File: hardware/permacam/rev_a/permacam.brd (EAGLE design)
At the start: 27 x 60 mm, 96 parts, among them J1 TC2030-JLINK-NL, Q1 PMDXB950UPEL, Q2 PMDXB950UPEL, Q3 PMDXB950UPEL, Q4 PMDXB950UPEL, Q5 PMDXB950UPEL, Q6 PMDXB950UPEL, U1 AB1815-T3, U10 NRF52840, U2 BQ25505, U3 EKMB1101111, U4 HM01B0-ANA, U6 SN74AUP2G04DCKRDCK6-L, U7 MAX17222, U8 MAX44009, X1 32MHz, X3 32.768kHz, X4 ABS07-32.768KHZ-7-T

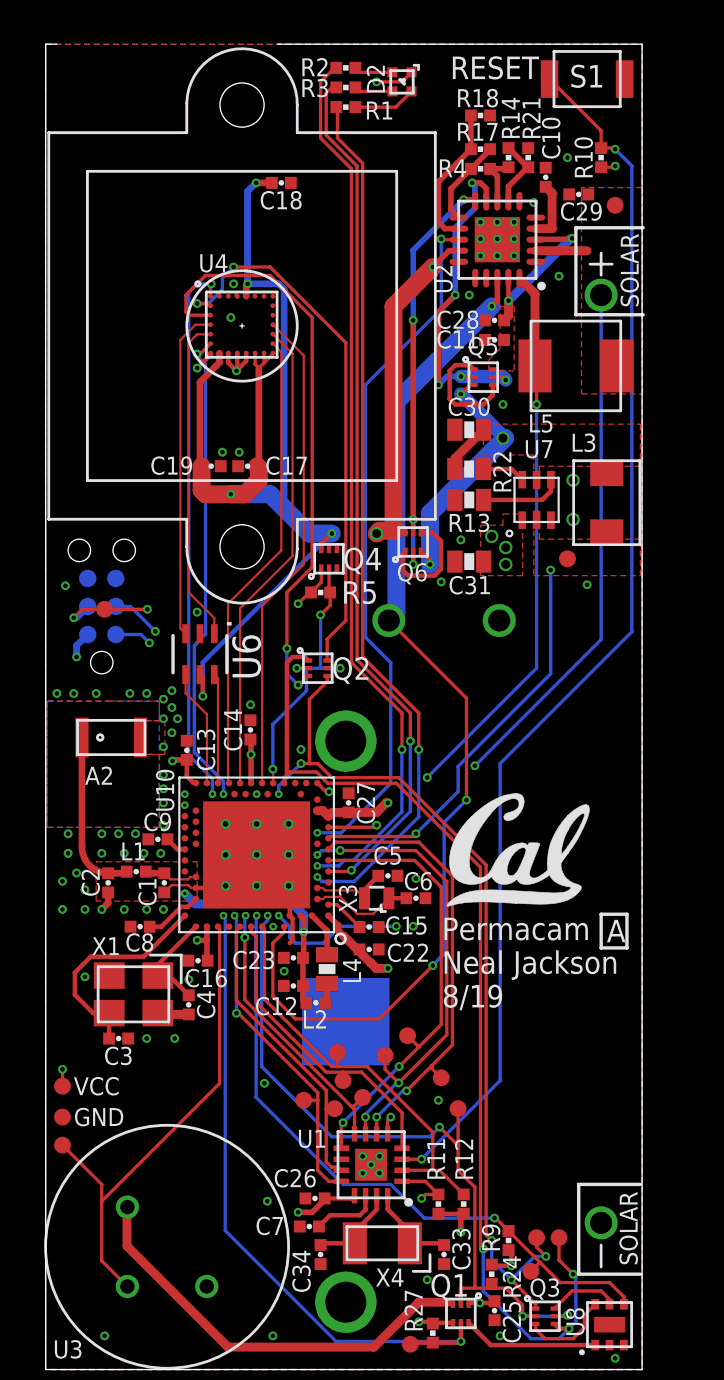
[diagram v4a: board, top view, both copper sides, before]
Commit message: fix exti floating
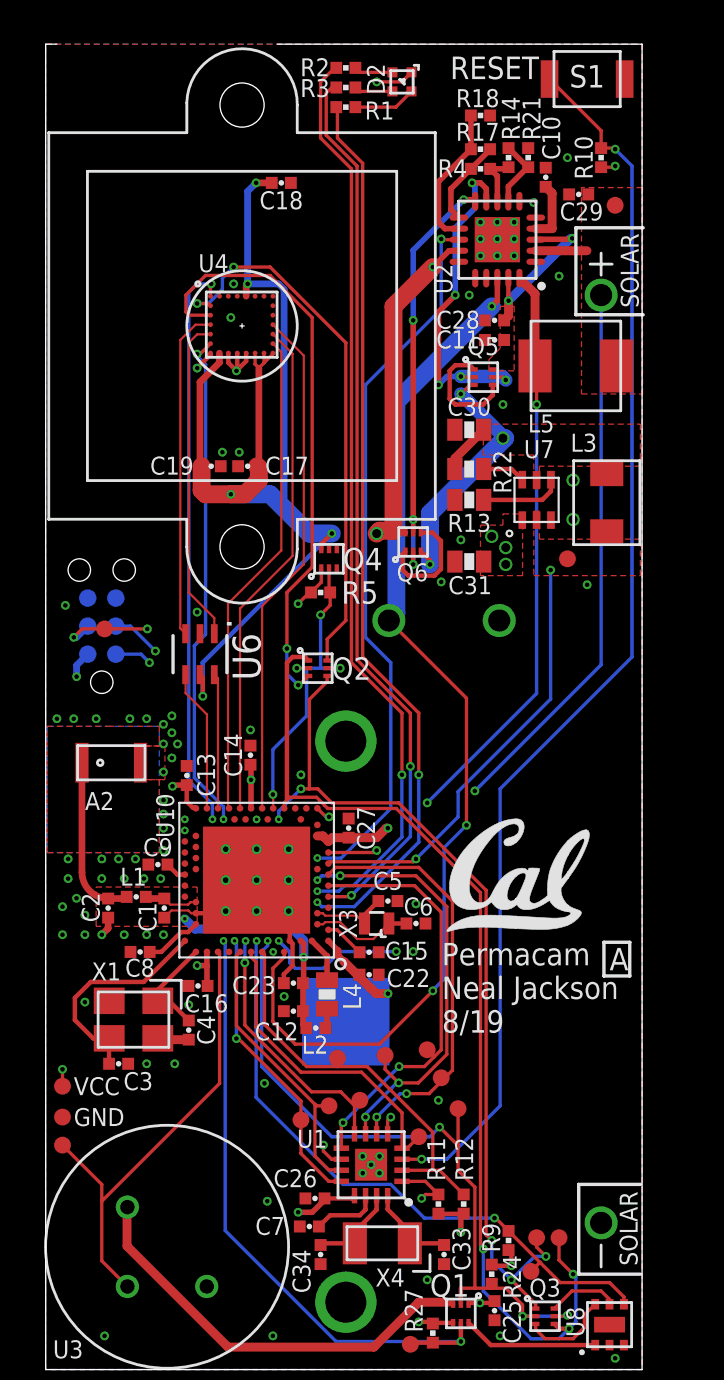
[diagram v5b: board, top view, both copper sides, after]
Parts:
- moved TP14 4.27 mm to (16.9, 10.5)
- moved A2 1.14 mm to (2.97, 27.5)
- moved C1 1.14 mm to (5.37, 20.9)
- moved C12 1.14 mm to (11.2, 16.2)
- moved C13 1.14 mm to (6.39, 26.9)
- moved C14 1.14 mm to (9.27, 27.8)
- moved C15 1.14 mm to (14.6, 18.9)
- moved C16 1.14 mm to (6.90, 17.4)
- moved C2 1.14 mm to (2.83, 20.9)
- moved C22 1.14 mm to (14.6, 17.9)
- moved C23 1.14 mm to (11.2, 17.5)
- moved C27 1.14 mm to (13.7, 24.5)
- moved C3 1.14 mm to (3.30, 13.8)
- moved C4 1.14 mm to (6.48, 15.4)
- moved C5 1.14 mm to (15.5, 21.2)
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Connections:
- net GND: now also U1.10
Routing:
- net RTC_CS: track 15.0 -> 13.3 mm
- net GND: track 20.4 -> 21.6 mm, vias 93 -> 94
- net VSOL: track 41.2 -> 42.3 mm
- net VSEC: track 47.3 -> 48.4 mm
- net VBAT_OK: track 31.6 -> 32.7 mm
- net PIR_OUT: track 22.3 -> 21.1 mm
- net PCLKO: track 21.7 -> 22.8 mm
- net MCLK: track 21.1 -> 22.2 mm
- net LVLD: track 5.31 -> 6.45 mm
- net LED_GREEN: track 40.4 -> 41.5 mm
- net LED_BLUE: track 39.5 -> 40.6 mm
- net LBST: track 30.4 -> 31.5 mm
- net FVLD: track 4.98 -> 6.12 mm
- net CAM_TRIG: track 21.6 -> 22.8 mm
- net CAM_INT: track 24.9 -> 26.1 mm
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
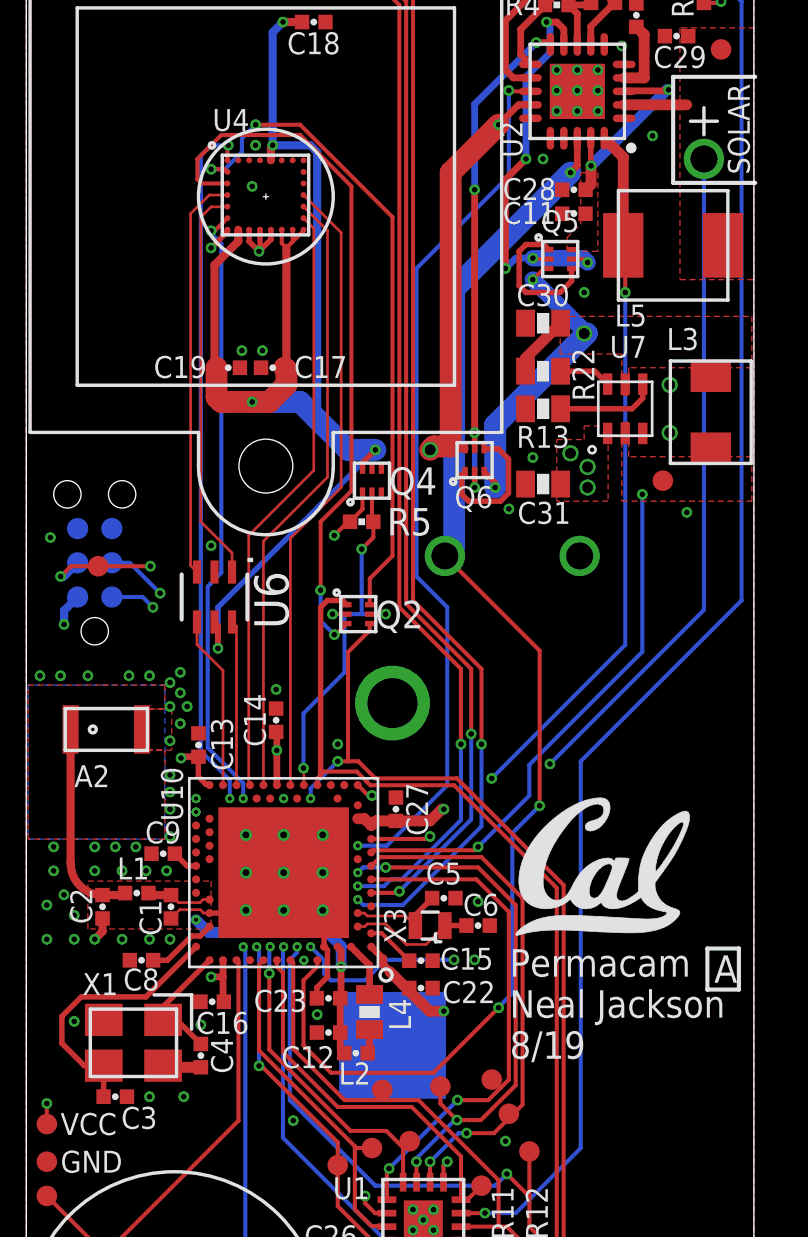
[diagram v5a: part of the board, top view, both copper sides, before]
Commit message: add debugging pads for camera signals
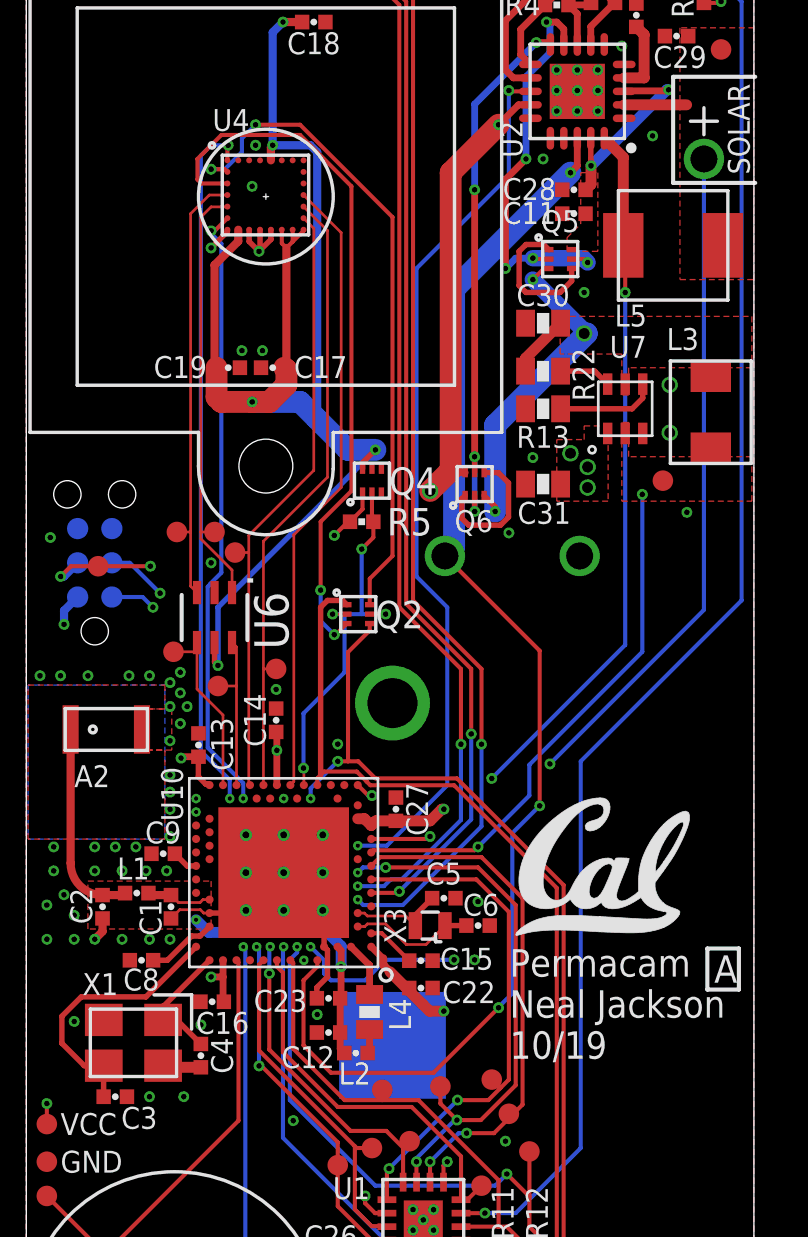
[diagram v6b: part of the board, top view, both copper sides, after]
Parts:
- added TP12, TP18, TP19, TP7, TP8, TP9: TEST-POINT, headers:PAD.03X.03
- moved Q6 0.89 mm to (16.6, 36.6)
- moved U6 0.76 mm to (6.99, 31.6)
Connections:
- net !FVLD: now also TP12.P$1
- net !LVLD: now also TP9.P$1
- net FVLD: now also TP8.P$1
- net LVLD: now also TP7.P$1
- net MCLK: now also TP19.P$1
- net PCLKO: now also TP18.P$1
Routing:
- net !LVLD: track 15.0 -> 16.3 mm
- net !FVLD: track 14.8 -> 16.1 mm
- net !VBAT_PRI_ON: track 19.2 -> 20.1 mm
- net VSW: track 13.9 -> 14.8 mm
- net MCLK: track 22.2 -> 22.7 mm
- net N$16: track 51.5 -> 52.0 mm
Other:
- board text added: "Permacam Neal Jackson 10/19"
- board text removed: "Permacam Neal Jackson 8/19"

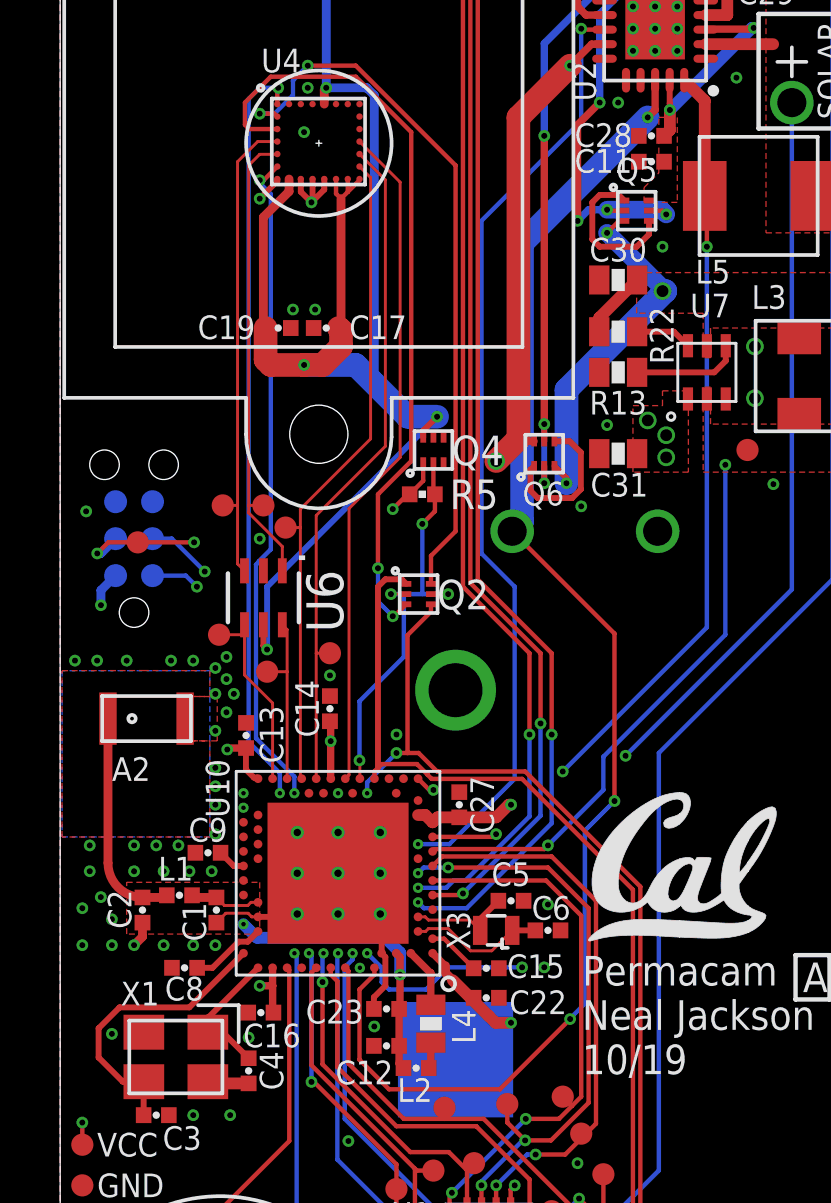
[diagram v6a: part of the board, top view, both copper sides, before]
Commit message: Add decoupling cap for camera supply
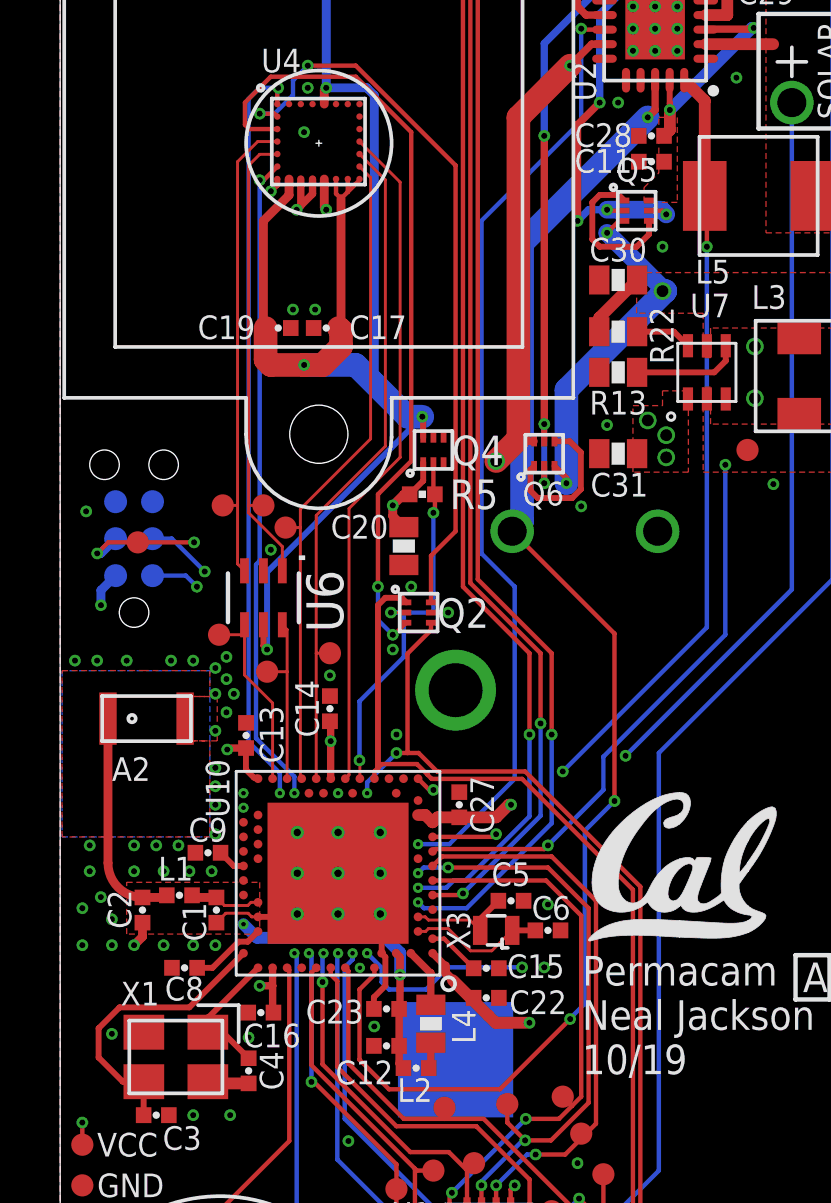
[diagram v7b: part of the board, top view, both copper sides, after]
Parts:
- added C20: 10uF, passives:0603_CAP
- moved Q2 0.64 mm to (12.3, 31.1)
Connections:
- net GND: now also C20.2
- net VCC: now also C20.1
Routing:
- net VCC: track 29.4 -> 30.9 mm
- net N$16: track 52.0 -> 51.1 mm
- net SDA: track 46.8 -> 46.1 mm
- net CAM_SDA: track 24.5 -> 25.1 mm
- net SCL: track 40.4 -> 39.8 mm
- net CAM_SCL: track 26.8 -> 27.4 mm
- net GND: track 21.6 -> 21.8 mm, vias 94 -> 97

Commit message: Implement will + josh changes
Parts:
- added R6, R7: DNP, passives:0402_RES
- added TP20, TP24, TP28, TP29: TEST-POINT, headers:PAD.03X.03
- moved TP17 4.60 mm to (0.76, 37.7)
- moved U$2 4.19 mm to (18.0, 24.0)
- moved TP7 0.64 mm to (4.83, 30.4)
- moved TP10 0.46 mm to (18.3, 11.6)
- moved C14 0.13 mm to (9.40, 27.8)
- flipped J1 to the top
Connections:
- net CAM_D0: now also TP20.P$1
- net CAM_D1: now also TP24.P$1
- net CAM_D2: now also TP28.P$1
- net CAM_D3: now also TP29.P$1
- net SCL: now also R7.1
- net SDA: now also R6.1
- net VCC: now also R6.2, R7.2
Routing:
- net N$16: track 51.1 -> 55.8 mm
- net !RST: track 38.9 -> 43.3 mm, vias 4 -> 3
- net CAM_D2: track 0.00 -> 2.54 mm, vias 0 -> 1
- net CAM_D1: track 0.00 -> 2.53 mm, vias 0 -> 1
- net CAM_D3: track 0.00 -> 2.36 mm, vias 0 -> 1
- net SCL: track 39.8 -> 42.0 mm
- net SWDIO: track 9.59 -> 11.6 mm
- net SWDCLK: track 11.3 -> 13.1 mm
- net VCC: track 30.9 -> 32.0 mm, vias 18 -> 19
- net CAM_D0: track 23.3 -> 24.1 mm
- net LVLD: track 6.56 -> 7.20 mm
- net !LT_EN: track 32.8 -> 32.2 mm
- net CAM_SCL: track 27.4 -> 28.0 mm
- net SDA: track 46.1 -> 46.7 mm
- net GND: vias 97 -> 121
